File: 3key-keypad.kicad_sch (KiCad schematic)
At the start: 19 parts

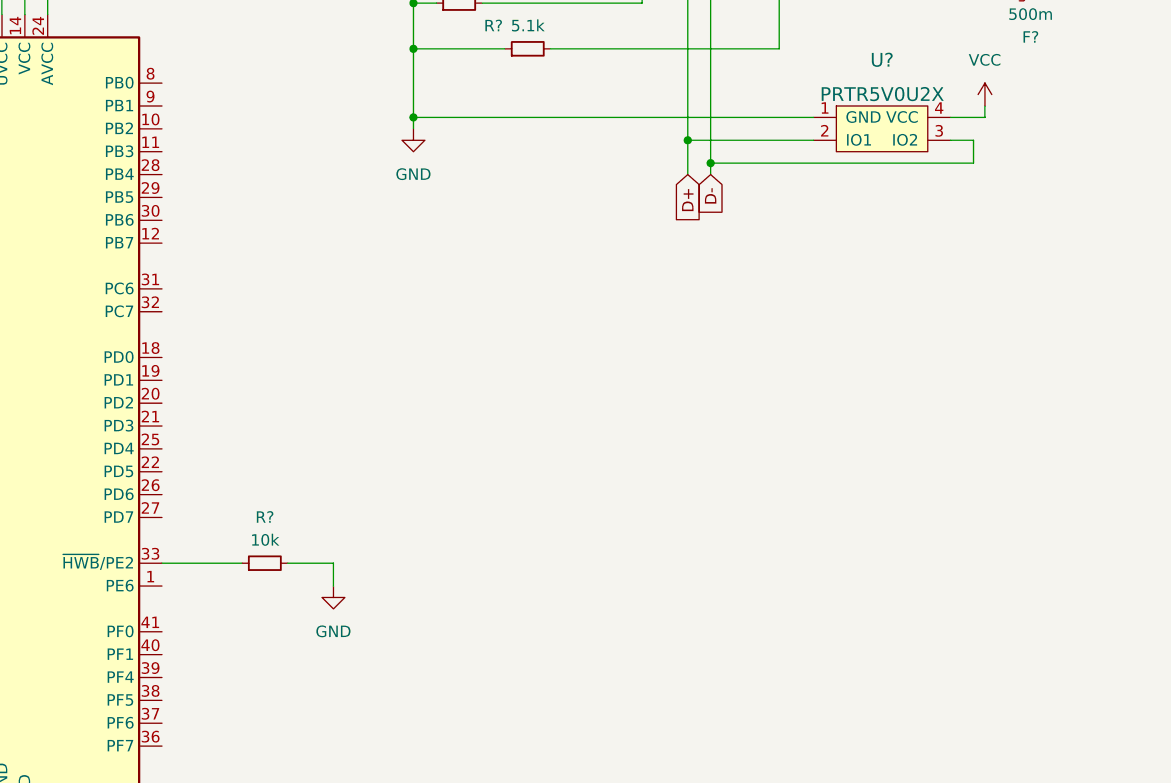
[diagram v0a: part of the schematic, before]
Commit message: added 2key matrix to schematic
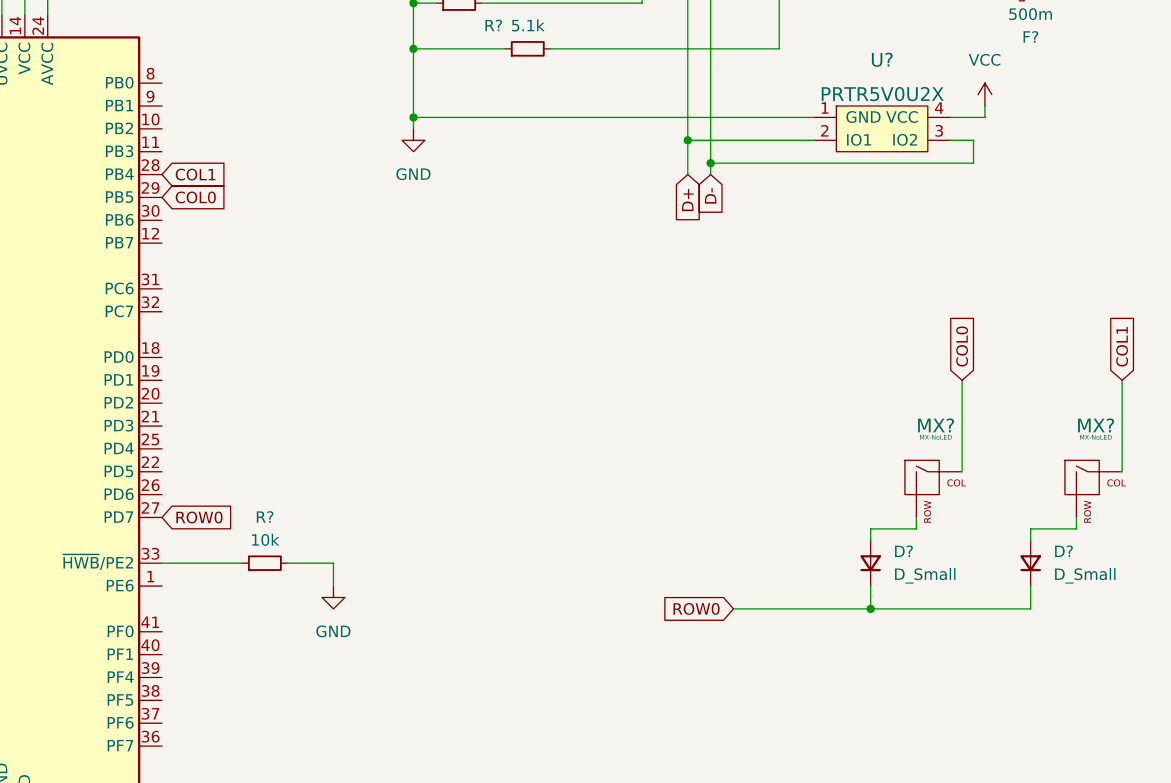
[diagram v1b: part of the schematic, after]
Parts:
- added D? (x2): D_Small, symbol Device:D_Small
- added MX? (x2): MX-NoLED, symbol MX_Alps_Hybrid:MX-NoLED
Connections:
- net ROW0: now reaches U?.27 (PD7)
- net ROW0: now also D?.1 (K), D?.1 (K)
- net COL1: now reaches U?.28 (PB4)
- net COL1: now also MX?.1 (COL)
- net COL0: now reaches U?.29 (PB5)
- net COL0: now also MX?.1 (COL)
- new net: D?.2 (A), MX?.2 (ROW) (x2)
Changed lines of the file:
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@@
   (junction (at 64.77 43.18) (diameter 0) (color 0 0 0 0)
+  )
+  (junction (at 176.53 110.49) (diameter 0) (color 0 0 0 0)
   )
   (junction (at 186.69 41.91) (diameter 0) (color 0 0 0 0)
@@
     (stroke (width 0) (type default) (color 0 0 0 0))
   )
+  (wire (pts (xy 194.31 101.6) (xy 199.39 101.6))
+    (stroke (width 0) (type default) (color 0 0 0 0))
+  )
   (wire (pts (xy 156.21 34.29) (xy 156.21 58.42))
     (stroke (width 0) (type default) (color 0 0 0 0))
@@
     (stroke (width 0) (type default) (color 0 0 0 0))
   )
+  (wire (pts (xy 194.31 107.95) (xy 194.31 110.49))
+    (stroke (width 0) (type default) (color 0 0 0 0))
+  )
   (wire (pts (xy 146.05 31.75) (xy 146.05 38.1))
     (stroke (width 0) (type default) (color 0 0 0 0))
@@
     (stroke (width 0) (type default) (color 0 0 0 0))
   )
+  (wire (pts (xy 176.53 102.87) (xy 176.53 101.6))
+    (stroke (width 0) (type default) (color 0 0 0 0))
+  )
   (wire (pts (xy 111.76 105.41) (xy 116.84 105.41))
     (stroke (width 0) (type default) (color 0 0 0 0))
@@
     (stroke (width 0) (type default) (color 0 0 0 0))
   )
+  (wire (pts (xy 204.47 85.09) (xy 204.47 95.25))
+    (stroke (width 0) (type default) (color 0 0 0 0))
+  )
   (wire (pts (xy 196.85 41.91) (xy 203.2 41.91))
     (stroke (width 0) (type default) (color 0 0 0 0))
@@
     (stroke (width 0) (type default) (color 0 0 0 0))
   )
+  (wire (pts (xy 194.31 110.49) (xy 176.53 110.49))
+    (stroke (width 0) (type default) (color 0 0 0 0))
+  )
   (wire (pts (xy 36.83 77.47) (xy 50.8 77.47))
     (stroke (width 0) (type default) (color 0 0 0 0))
@@
     (stroke (width 0) (type default) (color 0 0 0 0))
   )
+  (wire (pts (xy 176.53 101.6) (xy 181.61 101.6))
+    (stroke (width 0) (type default) (color 0 0 0 0))
+  )
   (wire (pts (xy 40.64 175.26) (xy 35.56 175.26))
     (stroke (width 0) (type default) (color 0 0 0 0))
@@
     (stroke (width 0) (type default) (color 0 0 0 0))
   )
+  (wire (pts (xy 176.53 107.95) (xy 176.53 110.49))
+    (stroke (width 0) (type default) (color 0 0 0 0))
+  )
+  (wire (pts (xy 199.39 101.6) (xy 199.39 100.33))
+    (stroke (width 0) (type default) (color 0 0 0 0))
+  )
+  (wire (pts (xy 181.61 101.6) (xy 181.61 100.33))
+    (stroke (width 0) (type default) (color 0 0 0 0))
+  )
   (wire (pts (xy 185.42 55.88) (xy 189.23 55.88))
     (stroke (width 0) (type default) (color 0 0 0 0))
@@
     (stroke (width 0) (type default) (color 0 0 0 0))
   )
+  (wire (pts (xy 194.31 102.87) (xy 194.31 101.6))
+    (stroke (width 0) (type default) (color 0 0 0 0))
+  )
   (wire (pts (xy 161.29 31.75) (xy 161.29 34.29))
     (stroke (width 0) (type default) (color 0 0 0 0))
@@
     (stroke (width 0) (type default) (color 0 0 0 0))
   )
+  (wire (pts (xy 186.69 85.09) (xy 186.69 95.25))
+    (stroke (width 0) (type default) (color 0 0 0 0))
+  )
   (wire (pts (xy 173.99 31.75) (xy 173.99 38.1))
     (stroke (width 0) (type default) (color 0 0 0 0))
@@
   )
   (wire (pts (xy 33.02 120.65) (xy 33.02 121.92))
+    (stroke (width 0) (type default) (color 0 0 0 0))
+  )
+  (wire (pts (xy 176.53 110.49) (xy 161.29 110.49))
     (stroke (width 0) (type default) (color 0 0 0 0))
   )
@@
     )
   )
+  (global_label "COL1" (shape input) (at 204.47 85.09 90) (fields_autoplaced)
+    (effects (font (size 1.27 1.27)) (justify left))
+    (property "Intersheet References" "${INTERSHEET_REFS}" (id 0) (at 204.3906 77.8388 90)
+      (effects (font (size 1.27 1.27)) (justify left) hide)
+    )
+  )
+  (global_label "COL0" (shape input) (at 97.79 64.77 0) (fields_autoplaced)
+    (effects (font (size 1.27 1.27)) (justify left))
+    (property "Intersheet References" "${INTERSHEET_REFS}" (id 0) (at 105.0412 64.6906 0)
+      (effects (font (size 1.27 1.27)) (justify left) hide)
+    )
+  )
+  (global_label "COL0" (shape input) (at 186.69 85.09 90) (fields_autoplaced)
+    (effects (font (size 1.27 1.27)) (justify left))
+    (property "Intersheet References" "${INTERSHEET_REFS}" (id 0) (at 186.6106 77.8388 90)
+      (effects (font (size 1.27 1.27)) (justify left) hide)
+    )
+  )
+  (global_label "ROW0" (shape input) (at 97.79 100.33 0) (fields_autoplaced)
+    (effects (font (size 1.27 1.27)) (justify left))
+    (property "Intersheet References" "${INTERSHEET_REFS}" (id 0) (at 105.4645 100.2506 0)
+      (effects (font (size 1.27 1.27)) (justify left) hide)
+    )
+  )
+  (global_label "COL1" (shape input) (at 97.79 62.23 0) (fields_autoplaced)
+    (effects (font (size 1.27 1.27)) (justify left))
+    (property "Intersheet References" "${INTERSHEET_REFS}" (id 0) (at 105.0412 62.1506 0)
+      (effects (font (size 1.27 1.27)) (justify left) hide)
+    )
+  )
   (global_label "XTAL1" (shape input) (at 55.88 57.15 180) (fields_autoplaced)
     (effects (font (size 1.27 1.27)) (justify right))
@@
     )
   )
+  (global_label "ROW0" (shape input) (at 161.29 110.49 180) (fields_autoplaced)
+    (effects (font (size 1.27 1.27)) (justify right))
+    (property "Intersheet References" "${INTERSHEET_REFS}" (id 0) (at 153.6155 110.4106 0)
+      (effects (font (size 1.27 1.27)) (justify right) hide)
+    )
+  )
   (global_label "D+" (shape input) (at 36.83 77.47 180) (fields_autoplaced)
     (effects (font (size 1.27 1.27)) (justify right))
@@
       (effects (font (size 1.27 1.27)) (justify right) hide)
     )
+  )
+  (symbol (lib_id "MX_Alps_Hybrid:MX-NoLED") (at 200.66 96.52 0) (unit 1)
+    (in_bom yes) (on_board yes) (fields_autoplaced)
+    (property "Reference" "MX?" (id 0) (at 201.5456 90.17 0)
+      (effects (font (size 1.524 1.524)))
+    )
+    (property "Value" "MX-NoLED" (id 1) (at 201.5456 91.44 0)
+      (effects (font (size 0.508 0.508)))
+    )
+    (property "Footprint" "" (id 2) (at 184.785 97.155 0)
+      (effects (font (size 1.524 1.524)) hide)
+    )
+    (property "Datasheet" "" (id 3) (at 184.785 97.155 0)
+      (effects (font (size 1.524 1.524)) hide)
+    )
+    (pin "1")
+    (pin "2")
   )
   (symbol (lib_id "Device:R_Small") (at 130.81 43.18 90) (unit 1)
@@
     )
     (pin "1")
+  )
+  (symbol (lib_id "Device:D_Small") (at 176.53 105.41 90) (unit 1)
+    (in_bom yes) (on_board yes) (fields_autoplaced)
+    (property "Reference" "D?" (id 0) (at 179.07 104.1399 90)
+      (effects (font (size 1.27 1.27)) (justify right))
+    )
+    (property "Value" "D_Small" (id 1) (at 179.07 106.6799 90)
+      (effects (font (size 1.27 1.27)) (justify right))
+    )
+    (property "Footprint" "" (id 2) (at 176.53 105.41 90)
+      (effects (font (size 1.27 1.27)) hide)
+    )
+    (property "Datasheet" "~" (id 3) (at 176.53 105.41 90)
+      (effects (font (size 1.27 1.27)) hide)
+    )
+    (pin "1")
+    (pin "2")
   )
   (symbol (lib_id "Device:C_Small") (at 57.15 90.17 0) (unit 1)
@@
     (pin "1")
   )
+  (symbol (lib_id "MX_Alps_Hybrid:MX-NoLED") (at 182.88 96.52 0) (unit 1)
+    (in_bom yes) (on_board yes) (fields_autoplaced)
+    (property "Reference" "MX?" (id 0) (at 183.7656 90.17 0)
+      (effects (font (size 1.524 1.524)))
+    )
+    (property "Value" "MX-NoLED" (id 1) (at 183.7656 91.44 0)
+      (effects (font (size 0.508 0.508)))
+    )
+    (property "Footprint" "" (id 2) (at 167.005 97.155 0)
+      (effects (font (size 1.524 1.524)) hide)
+    )
+    (property "Datasheet" "" (id 3) (at 167.005 97.155 0)
+      (effects (font (size 1.524 1.524)) hide)
+    )
+    (pin "1")
+    (pin "2")
+  )
   (symbol (lib_id "power:GND") (at 125.73 57.15 0) (unit 1)
     (in_bom yes) (on_board yes) (fields_autoplaced)
@@
     )
     (pin "1")
+  )
+  (symbol (lib_id "Device:D_Small") (at 194.31 105.41 90) (unit 1)
+    (in_bom yes) (on_board yes) (fields_autoplaced)
+    (property "Reference" "D?" (id 0) (at 196.85 104.1399 90)
+      (effects (font (size 1.27 1.27)) (justify right))
+    )
+    (property "Value" "D_Small" (id 1) (at 196.85 106.6799 90)
+      (effects (font (size 1.27 1.27)) (justify right))
+    )
+    (property "Footprint" "" (id 2) (at 194.31 105.41 90)
+      (effects (font (size 1.27 1.27)) hide)
+    )
+    (property "Datasheet" "~" (id 3) (at 194.31 105.41 90)
+      (effects (font (size 1.27 1.27)) hide)
+    )
+    (pin "1")
+    (pin "2")
   )
   (symbol (lib_id "Device:C_Small") (at 31.75 171.45 0) (unit 1)
@@
       (reference "C?") (unit 1) (value "10uF") (footprint "")
     )
+    (path "/604dc8a5-dc9d-42c8-9486-cb131767af65"
+      (reference "D?") (unit 1) (value "D_Small") (footprint "")
+    )
+    (path "/873b6378-7389-4f90-a46b-173d47538a3d"
+      (reference "D?") (unit 1) (value "D_Small") (footprint "")
+    )
     (path "/21c265ba-e3f3-4338-b04e-b3cf73b8be86"
       (reference "F?") (unit 1) (value "500m") (footprint "")
     )
+    (path "/04b699f2-3c0f-474e-bf36-993bcf5c0a1f"
+      (reference "MX?") (unit 1) (value "MX-NoLED") (footprint "")
+    )
+    (path "/73744e51-3909-4238-8142-53721c8ec829"
+      (reference "MX?") (unit 1) (value "MX-NoLED") (footprint "")
+    )
     (path "/0f7e0689-1cf3-419a-b20f-cca541f18dc2"

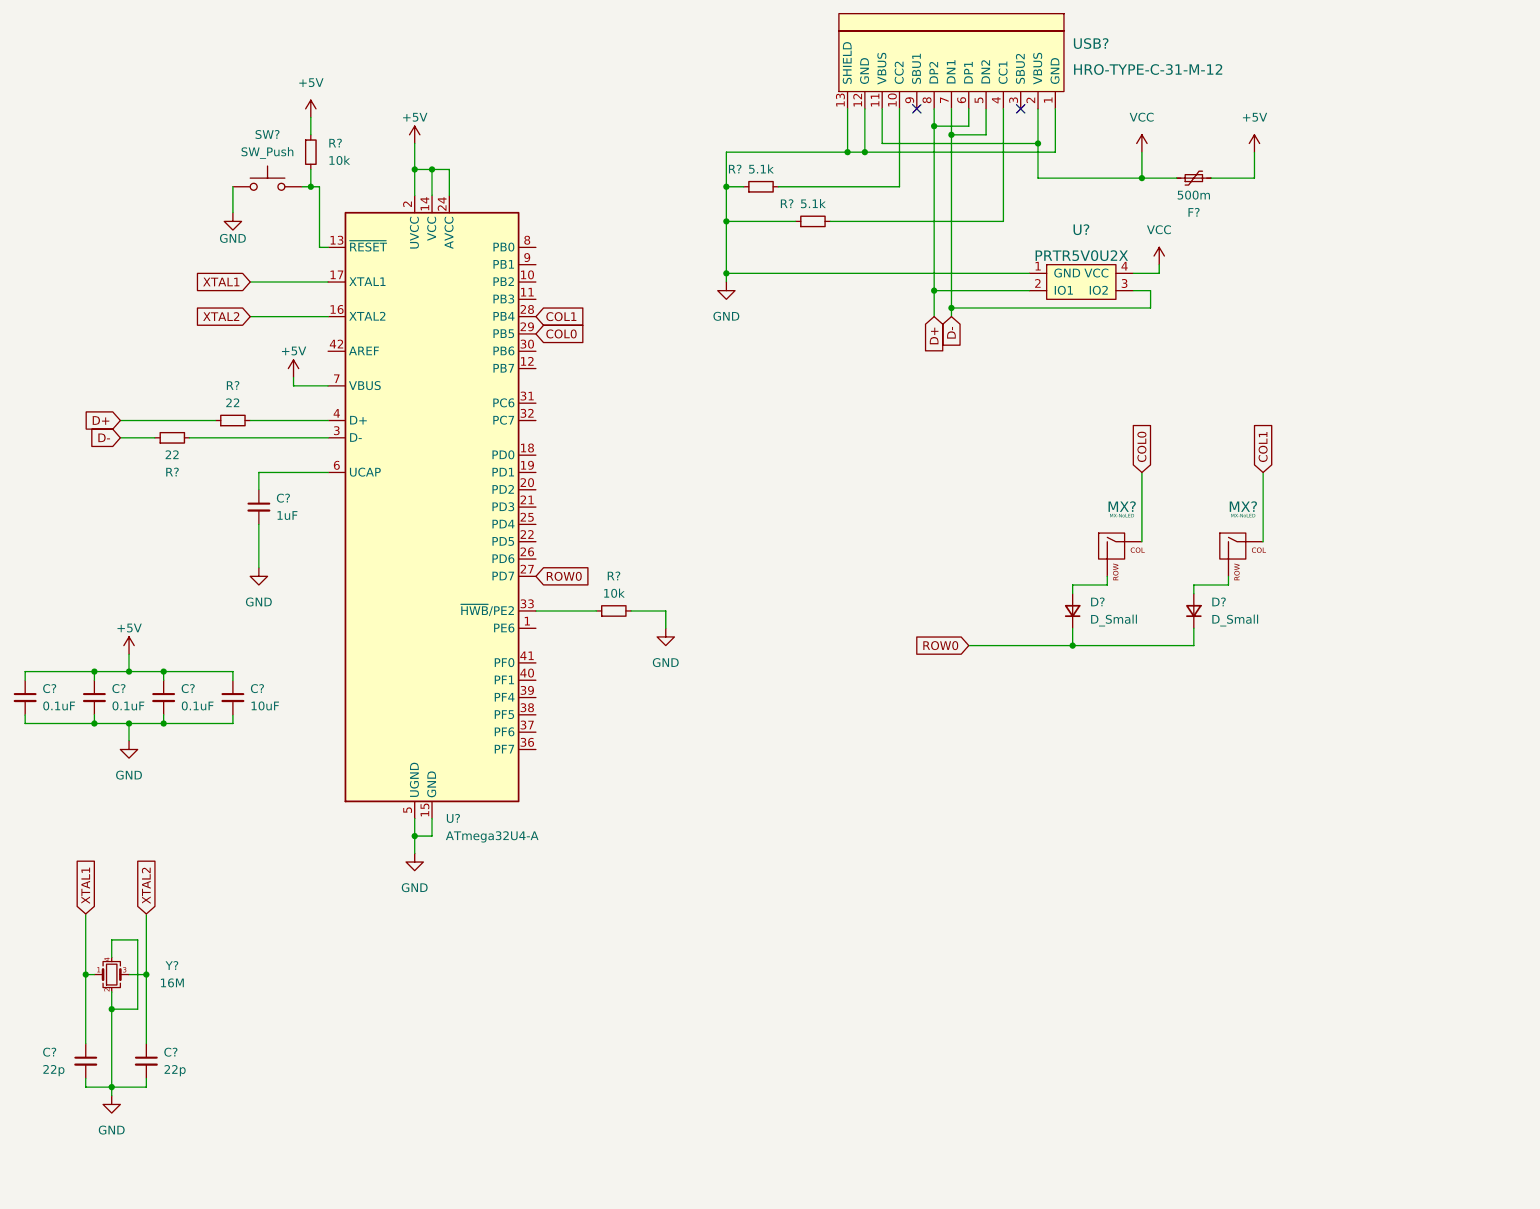
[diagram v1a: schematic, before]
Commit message: assigned footprints and made basic layout
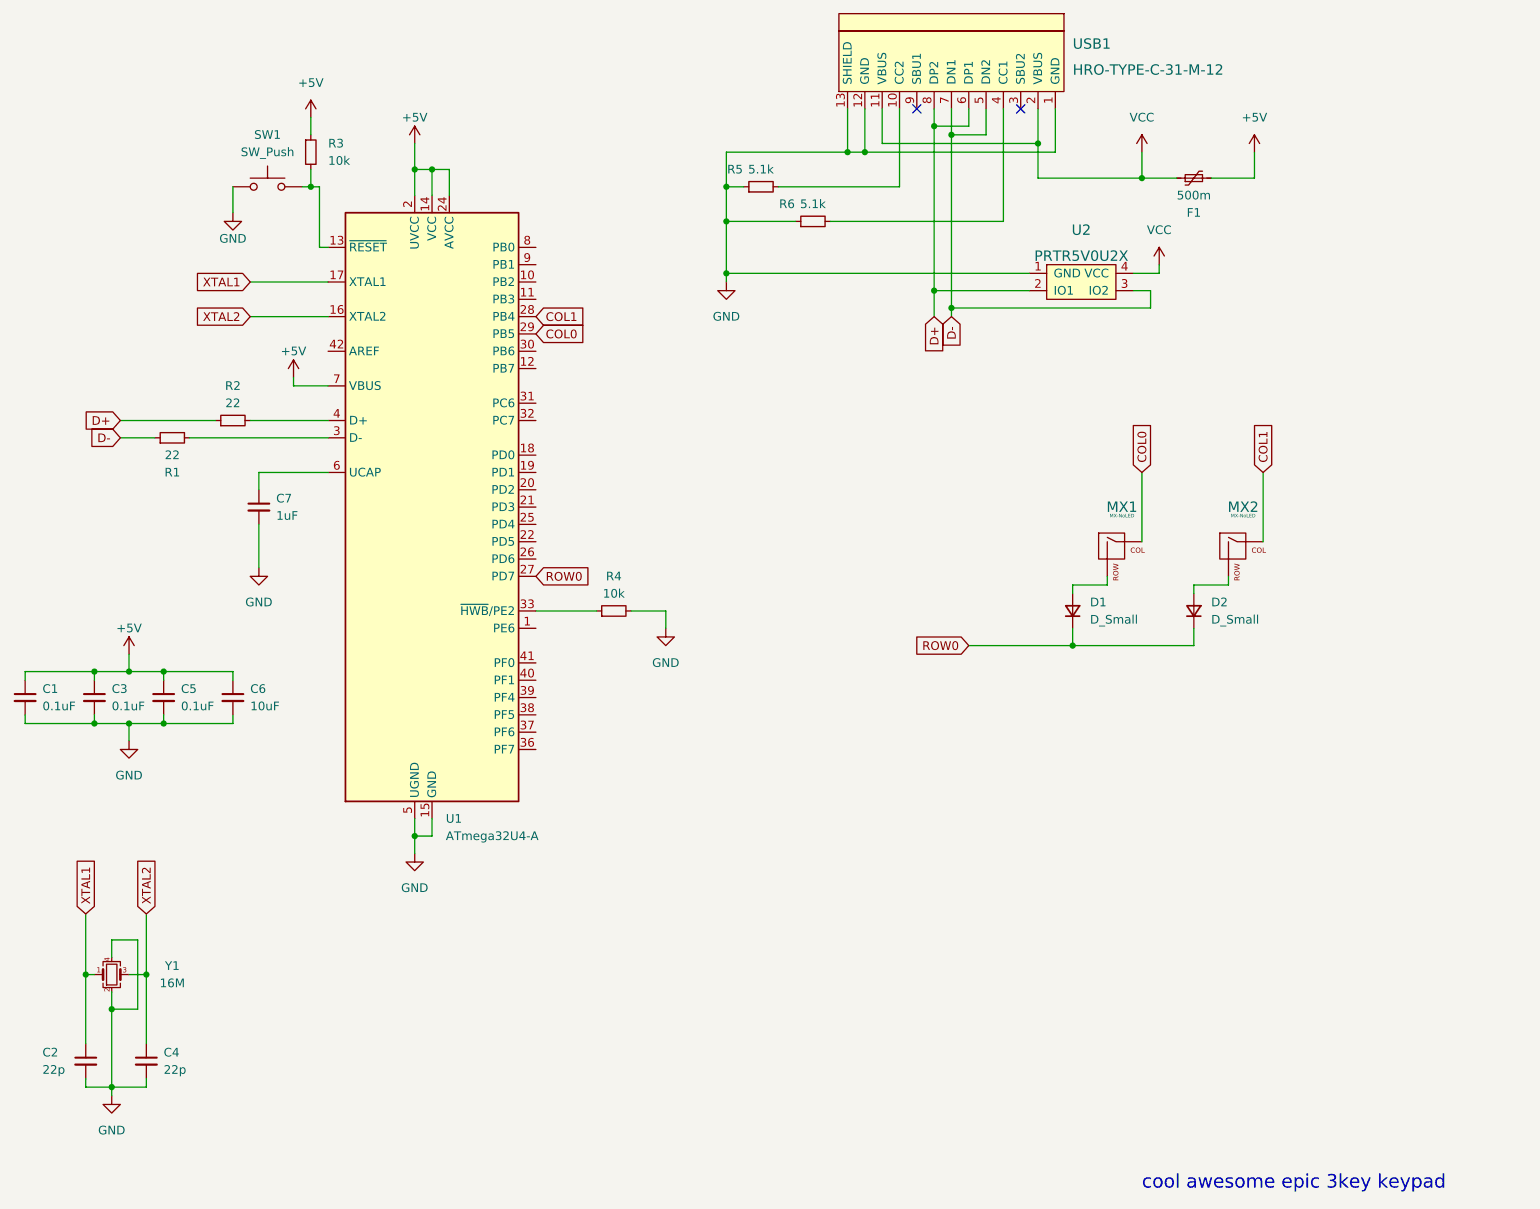
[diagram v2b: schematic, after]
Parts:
- C1, C2, C3, C4, C5, C6, C7: renamed from C?; footprint (none) -> Capacitor_SMD:C_0805_2012Metric
- D1, D2: renamed from D?; footprint (none) -> Diode_SMD:D_SOD-123
- F1: renamed from F?; footprint (none) -> Fuse:Fuse_1206_3216Metric
- MX1, MX2: renamed from MX?; footprint (none) -> MX_Alps_Hybrid:MX-1U-NoLED
- R1, R2, R3, R4, R5, R6: renamed from R?; footprint (none) -> Resistor_SMD:R_0805_2012Metric
- SW1: renamed from SW?; footprint (none) -> random-keyboard-parts:SKQG-1155865
- U2: renamed from U?; footprint (none) -> random-keyboard-parts:SOT143B
- USB1: renamed from USB?; footprint (none) -> Type-C:HRO-TYPE-C-31-M-12-HandSoldering
- Y1: renamed from Y?; footprint (none) -> Crystal:Crystal_SMD_3225-4Pin_3.2x2.5mm
- gave numbers to parts that had none: 1
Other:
- note added: "cool awesome epic 3key keypad"
